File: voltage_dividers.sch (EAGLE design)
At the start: 17 parts, among them X1 OPAMP, X2 OPAMP

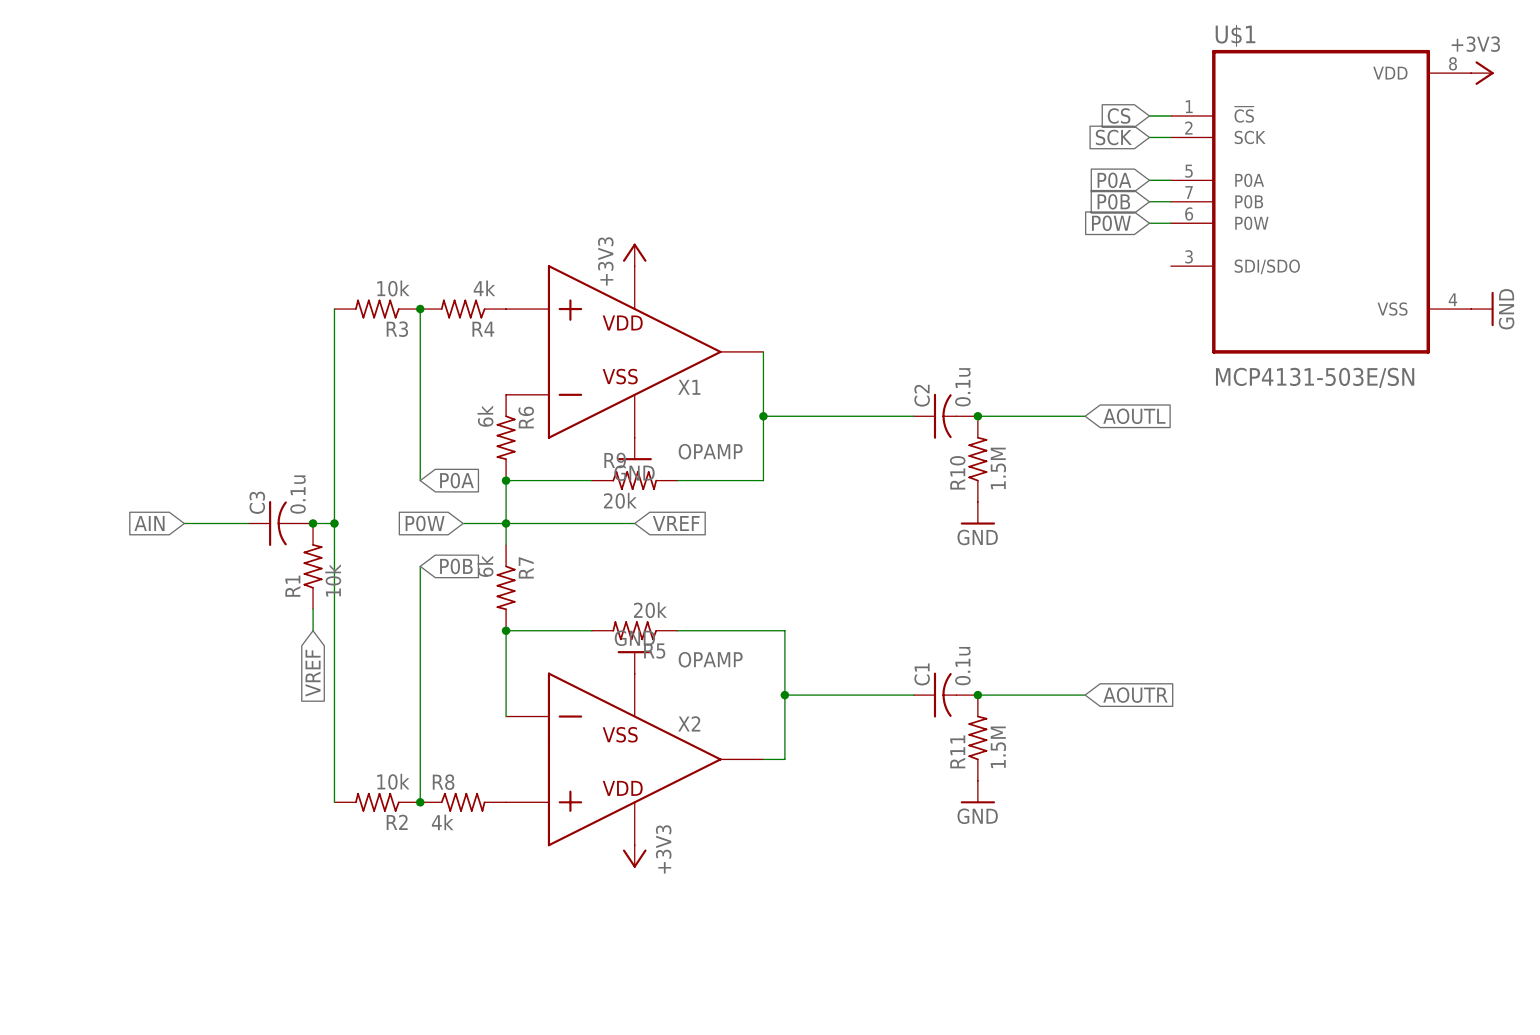
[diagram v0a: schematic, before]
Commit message: rm cache files, add boards for components
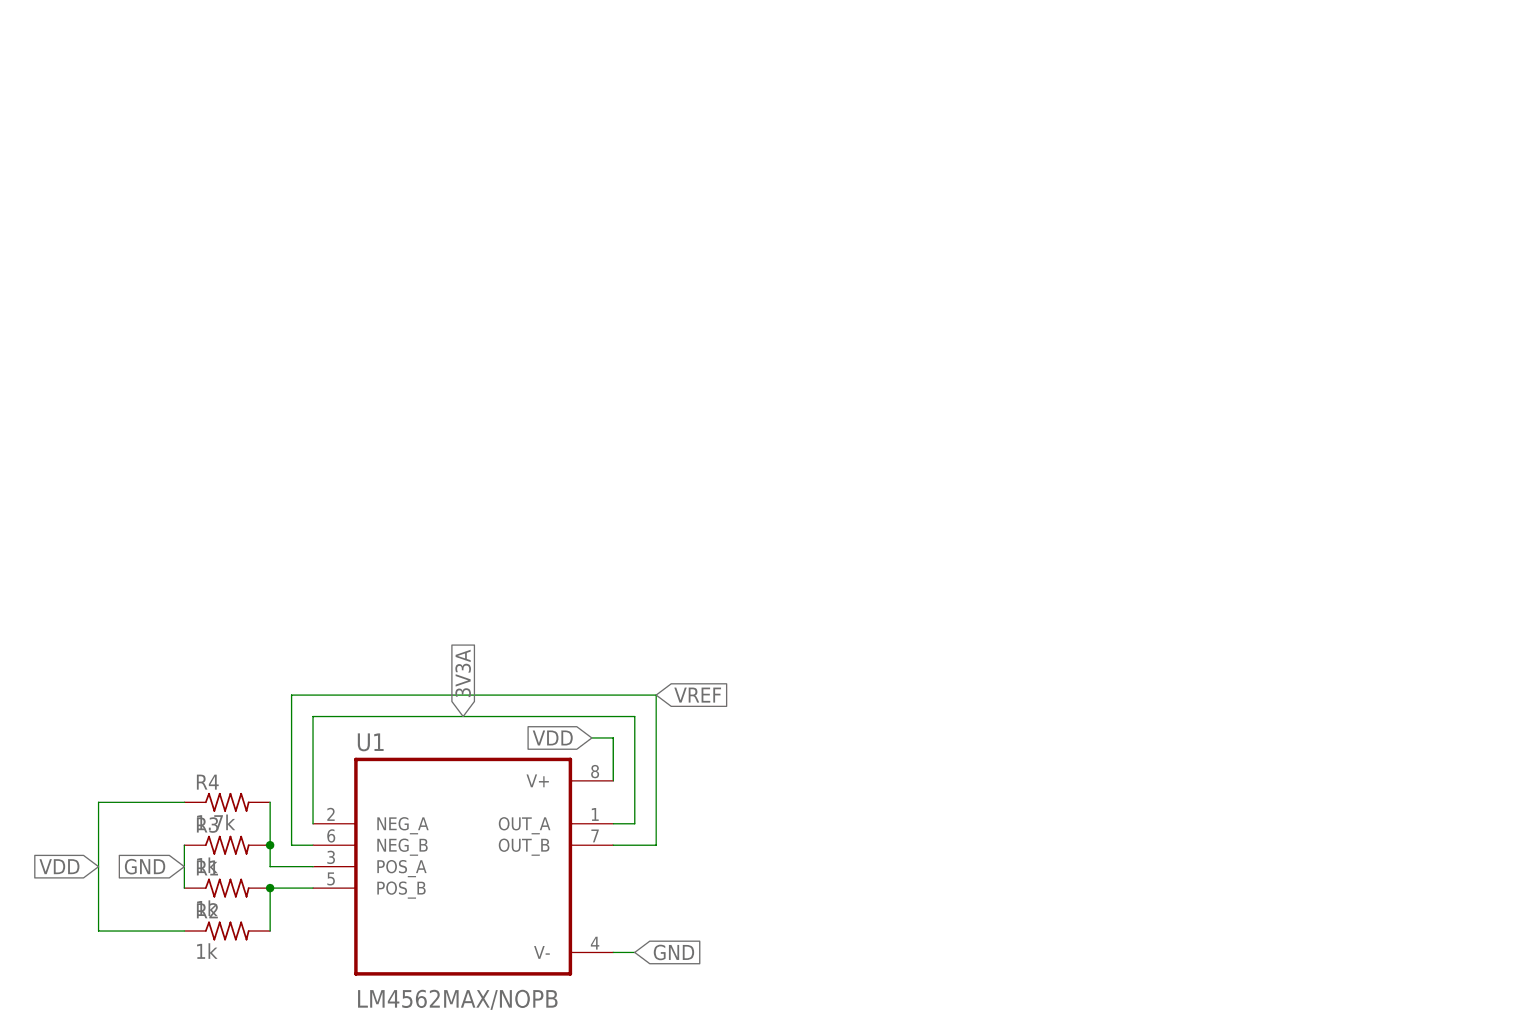
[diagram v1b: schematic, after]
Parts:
- removed C1, C2, C3: 0.1u, rcl:C-US025-024X044
- removed R10, R11: 1.5M, rcl:R-US_0204/5
- removed R5, R9: 20k, rcl:R-US_0204/5
- removed R6, R7: 6k, rcl:R-US_0204/5
- removed R8: 4k, rcl:R-US_0204/5
- removed U$1: MCP4131-503E/SN, MCP4131-503E_SN:MCP4131-503E/SN
- removed X1, X2: OPAMP, ngspice-simulation:OPAMP
- added U1: LM4562MAX/NOPB, LM4562MAX_NOPB:LM4562MAX/NOPB
- R1, R2, R3: value 10k -> 1k; device rcl:R-US_0204/5 -> rcl:R-US_R0402
- R4: value 4k -> 1.7k; device rcl:R-US_0204/5 -> rcl:R-US_R0402
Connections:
- removed net +3V3: U$1.VDD, X1.VDD, X2.VDD
- removed net AIN: C3.1
- removed net AOUTL: C2.2, R10.2
- removed net AOUTR: C1.2, R11.2
- removed net CS: U$1.!CS
- removed net N$12: R8.2, X2.P
- removed net N$13: R4.1, X1.P
- removed net N$6: R6.1, X1.N
- removed net N$7: R5.2, R7.2, X2.N
- removed net N$8: C1.1, R5.1, X2.VOUT
- removed net N$9: C2.1, R9.2, X1.VOUT
- removed net P0A: R3.1, R4.2, U$1.P0A
- removed net P0B: R2.1, R8.1, U$1.P0B
- removed net P0W: R6.2, R7.1, R9.1, U$1.P0W
- removed net SCK: U$1.SCK
- new net 3V3A: U1.NEG_A, U1.OUT_A
- new net N$1: R3.2, R4.2, U1.POS_A
- new net VDD: R2.1, R4.1, U1.V+
- net GND: now also R1.1, R3.1, U1.V-; no longer R10.1, R11.1, U$1.VSS, X1.VSS, X2.VSS
- net N$2: now also U1.POS_B; no longer C3.2, R3.2
- net VREF: now also U1.NEG_B, U1.OUT_B; no longer R1.1
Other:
- moved on the sheet: R1, R2, R3, R4

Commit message: corrections
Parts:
- added 9VDD, GND: (no value), wirepad:SMD2
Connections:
- net GND: now also GND.P
- net VDD: now also 9VDD.P
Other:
- moved on the sheet: R1, R2, R4
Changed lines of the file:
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@@
 <layer number="97" name="Info" color="7" fill="1" visible="yes" active="yes"/>
 <layer number="98" name="Guide" color="6" fill="1" visible="yes" active="yes"/>
+<layer number="99" name="SpiceOrder" color="7" fill="1" visible="yes" active="yes"/>
 </layers>
 <schematic xreflabel="%F%N/%S.%C%R" xrefpart="/%S.%C%R">
@@
 <class number="0" name="default" width="0" drill="0">
 </class>
-<class number="1" name="ANALOG" width="0.508" drill="0.508">
-<clearance class="1" value="0.254"/>
-</class>
-<class number="2" name="POWER" width="0.508" drill="0.508">
-<clearance class="2" value="0.254"/>
-</class>
-<class number="3" name="GND" width="0.508" drill="0.508">
-<clearance class="3" value="0.254"/>
-</class>
 </classes>
 <parts>
@@
 <part name="R3" library="rcl" library_urn="urn:adsk.eagle:library:334" deviceset="R-US_" device="R0402" package3d_urn="urn:adsk.eagle:package:23547/3" value="1k"/>
 <part name="R4" library="rcl" library_urn="urn:adsk.eagle:library:334" deviceset="R-US_" device="R0402" package3d_urn="urn:adsk.eagle:package:23547/3" value="1.7k"/>
+<part name="9VDD" library="wirepad" library_urn="urn:adsk.eagle:library:412" deviceset="SMD2" device="" package3d_urn="urn:adsk.eagle:package:30839/1"/>
+<part name="GND" library="wirepad" library_urn="urn:adsk.eagle:library:412" deviceset="SMD2" device="" package3d_urn="urn:adsk.eagle:package:30839/1"/>
 </parts>
 <sheets>
@@
 <attribute name="VALUE" x="12.7" y="3.62" size="2.0828" layer="96" ratio="10" rot="SR0"/>
 </instance>
-<instance part="R1" gate="G$1" x="-2.54" y="17.78" smashed="yes">
-<attribute name="NAME" x="-6.35" y="19.2786" size="1.778" layer="95"/>
-<attribute name="VALUE" x="-6.35" y="14.478" size="1.778" layer="96"/>
+<instance part="R1" gate="G$1" x="-2.54" y="15.24" smashed="yes">
+<attribute name="NAME" x="-6.35" y="16.7386" size="1.778" layer="95"/>
+<attribute name="VALUE" x="-6.35" y="11.938" size="1.778" layer="96"/>
 </instance>
-<instance part="R2" gate="G$1" x="-2.54" y="12.7" smashed="yes">
-<attribute name="NAME" x="-6.35" y="14.1986" size="1.778" layer="95"/>
-<attribute name="VALUE" x="-6.35" y="9.398" size="1.778" layer="96"/>
+<instance part="R2" gate="G$1" x="-2.54" y="7.62" smashed="yes">
+<attribute name="NAME" x="-6.35" y="9.1186" size="1.778" layer="95"/>
+<attribute name="VALUE" x="-6.35" y="4.318" size="1.778" layer="96"/>
 </instance>
 <instance part="R3" gate="G$1" x="-2.54" y="22.86" smashed="yes">
@@
 <attribute name="VALUE" x="-6.35" y="19.558" size="1.778" layer="96"/>
 </instance>
-<instance part="R4" gate="G$1" x="-2.54" y="27.94" smashed="yes">
-<attribute name="NAME" x="-6.35" y="29.4386" size="1.778" layer="95"/>
-<attribute name="VALUE" x="-6.35" y="24.638" size="1.778" layer="96"/>
+<instance part="R4" gate="G$1" x="-2.54" y="30.48" smashed="yes">
+<attribute name="NAME" x="-6.35" y="31.9786" size="1.778" layer="95"/>
+<attribute name="VALUE" x="-6.35" y="27.178" size="1.778" layer="96"/>
+</instance>
+<instance part="9VDD" gate="1" x="-20.32" y="22.86" smashed="yes">
+<attribute name="NAME" x="-21.463" y="24.7142" size="1.778" layer="95"/>
+<attribute name="VALUE" x="-21.463" y="19.558" size="1.778" layer="96"/>
+</instance>
+<instance part="GND" gate="1" x="45.72" y="7.62" smashed="yes" rot="R90">
+<attribute name="NAME" x="43.8658" y="6.477" size="1.778" layer="95" rot="R90"/>
+<attribute name="VALUE" x="49.022" y="6.477" size="1.778" layer="96" rot="R90"/>
 </instance>
 </instances>
@@
 </busses>
 <nets>
-<net name="N$1" class="1">
+<net name="N$1" class="0">
 <segment>
 <pinref part="U1" gate="A" pin="POS_A"/>
@@
 <pinref part="R3" gate="G$1" pin="2"/>
 <pinref part="R4" gate="G$1" pin="2"/>
-<wire x1="2.54" y1="22.86" x2="2.54" y2="27.94" width="0.1524" layer="91"/>
+<wire x1="2.54" y1="22.86" x2="2.54" y2="30.48" width="0.1524" layer="91"/>
 <junction x="2.54" y="22.86"/>
 </segment>
 </net>
-<net name="N$2" class="1">
+<net name="N$2" class="0">
 <segment>
 <pinref part="U1" gate="A" pin="POS_B"/>
-<wire x1="7.62" y1="17.78" x2="2.54" y2="17.78" width="0.1524" layer="91"/>
-<wire x1="2.54" y1="17.78" x2="2.54" y2="12.7" width="0.1524" layer="91"/>
+<wire x1="7.62" y1="17.78" x2="2.54" y2="15.24" width="0.1524" layer="91"/>
+<wire x1="2.54" y1="15.24" x2="2.54" y2="7.62" width="0.1524" layer="91"/>
 <pinref part="R2" gate="G$1" pin="2"/>
 <pinref part="R1" gate="G$1" pin="2"/>
-<junction x="2.54" y="17.78"/>
+<junction x="2.54" y="15.24"/>
 </segment>
 </net>
-<net name="GND" class="3">
+<net name="GND" class="0">
 <segment>
 <pinref part="R3" gate="G$1" pin="1"/>
 <pinref part="R1" gate="G$1" pin="1"/>
-<wire x1="-7.62" y1="22.86" x2="-7.62" y2="17.78" width="0.1524" layer="91"/>
+<wire x1="-7.62" y1="22.86" x2="-7.62" y2="15.24" width="0.1524" layer="91"/>
 <label x="-7.62" y="20.32" size="1.778" layer="95" rot="R180" xref="yes"/>
 </segment>
@@
 <wire x1="43.18" y1="10.16" x2="45.72" y2="10.16" width="0.1524" layer="91"/>
 <label x="45.72" y="10.16" size="1.778" layer="95" xref="yes"/>
+<pinref part="GND" gate="1" pin="P"/>
 </segment>
 </net>
-<net name="VDD" class="2">
+<net name="VDD" class="0">
 <segment>
 <pinref part="R4" gate="G$1" pin="1"/>
-<wire x1="-7.62" y1="27.94" x2="-17.78" y2="27.94" width="0.1524" layer="91"/>
+<wire x1="-7.62" y1="30.48" x2="-17.78" y2="27.94" width="0.1524" layer="91"/>
 <pinref part="R2" gate="G$1" pin="1"/>
-<wire x1="-17.78" y1="27.94" x2="-17.78" y2="12.7" width="0.1524" layer="91"/>
-<wire x1="-17.78" y1="12.7" x2="-7.62" y2="12.7" width="0.1524" layer="91"/>
+<wire x1="-17.78" y1="27.94" x2="-17.78" y2="22.86" width="0.1524" layer="91"/>
+<wire x1="-17.78" y1="22.86" x2="-17.78" y2="12.7" width="0.1524" layer="91"/>
+<wire x1="-17.78" y1="12.7" x2="-7.62" y2="7.62" width="0.1524" layer="91"/>
 <label x="-17.78" y="20.32" size="1.778" layer="95" rot="R180" xref="yes"/>
+<pinref part="9VDD" gate="1" pin="P"/>
+<junction x="-17.78" y="22.86"/>
 </segment>
 <segment>
@@
 </segment>
 </net>
-<net name="3V3A" class="2">
+<net name="3V3A" class="0">
 <segment>
 <pinref part="U1" gate="A" pin="NEG_A"/>
@@
 </segment>
 </net>
-<net name="VREF" class="2">
+<net name="VREF" class="0">
 <segment>
 <pinref part="U1" gate="A" pin="NEG_B"/>
